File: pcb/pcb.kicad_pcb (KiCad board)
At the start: 2 copper layers, 57 x 84 mm, 4 parts, among them J1 Botones, J2 Pedales+Velocimetro+Monedas, J3 Volante

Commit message: Add layout and schematic prints
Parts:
- moved A1 70.9 mm to (99.1, 147.3)
- moved J1 70.9 mm to (89.9, 179.1)
- moved J2 70.9 mm to (109.2, 102.4)
- moved J3 70.9 mm to (106.7, 111.8)
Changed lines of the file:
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@@
     (thickness 1.6)
   )
-  (paper "A4")
+  (paper "A4" portrait)
+  (title_block
+    (title "Ches Pur Ofi")
+    (date "3/2021")
+    (rev "V1")
+  )
   (layers
     (0 "F.Cu" signal)
@@
   (net 32 "Net-(A1-Pad32)")
   (footprint "Connector_PinSocket_2.54mm:PinSocket_1x03_P2.54mm_Vertical" (layer "F.Cu")
-    (at 157.48 62.23 90)
+    (at 106.68 111.76 90)
     (descr "Through hole straight socket strip, 1x03, 2.54mm pitch, single row (from Kicad 4.0.7), script generated")
     (tags "Through hole socket strip THT 1x03 2.54mm single row")
@@
   )
   (footprint "luqas11:Arduino_Leonardo_WithFemaleSockets" (layer "F.Cu")
-    (at 149.86 97.79)
+    (at 99.06 147.32)
     (attr through_hole)
     (fp_text reference "A1" (at 0 0.5) (layer "F.SilkS")
@@
   )
   (footprint "Connector_PinSocket_2.54mm:PinSocket_1x08_P2.54mm_Vertical" (layer "F.Cu")
-    (at 140.716 129.54 90)
+    (at 89.916 179.07 90)
     (descr "Through hole straight socket strip, 1x08, 2.54mm pitch, single row (from Kicad 4.0.7), script generated")
     (tags "Through hole socket strip THT 1x08 2.54mm single row")
@@
   )
   (footprint "Connector_PinSocket_2.54mm:PinSocket_1x06_P2.54mm_Vertical" (layer "F.Cu")
-    (at 160.02 52.832 90)
+    (at 109.22 102.362 90)
     (descr "Through hole straight socket strip, 1x06, 2.54mm pitch, single row (from Kicad 4.0.7), script generated")
     (tags "Through hole socket strip THT 1x06 2.54mm single row")
@@
     )
   )
-  (gr_line (start 128 49) (end 185 49)
+  (gr_line (start 77.2 98.53) (end 134.2 98.53)
     (stroke (width 0.1) (type solid)) (layer "Edge.Cuts"))
-  (gr_line (start 185 49) (end 185 133)
+  (gr_line (start 134.2 98.53) (end 134.2 182.53)
     (stroke (width 0.1) (type solid)) (layer "Edge.Cuts"))
-  (gr_line (start 185 133) (end 128 133)
+  (gr_line (start 134.2 182.53) (end 77.2 182.53)
     (stroke (width 0.1) (type solid)) (layer "Edge.Cuts"))
-  (gr_line (start 128 133) (end 128 49)
+  (gr_line (start 77.2 182.53) (end 77.2 98.53)
     (stroke (width 0.1) (type solid)) (layer "Edge.Cuts"))
-  (gr_text "V1 - 3/2021" (at 173 129) (layer "B.Cu")
+  (gr_text "V1 - 3/2021" (at 122.2 178.53) (layer "B.Cu")
     (effects (font (size 2 2) (thickness 0.5)) (justify mirror))
   )
-  (gr_text "DAYTONA" (at 154 94) (layer "B.Cu")
+  (gr_text "DAYTONA" (at 103.2 143.53) (layer "B.Cu")
     (effects (font (size 7 7) (thickness 1.3) italic) (justify mirror))
   )
-  (segment (start 138.18 127.004) (end 140.716 129.54) (width 1) (layer "B.Cu") (net 5))
-  (segment (start 138.18 120.65) (end 138.18 127.004) (width 1) (layer "B.Cu") (net 5))
-  (segment (start 143.26 129.536) (end 143.256 129.54) (width 1) (layer "B.Cu") (net 9))
-  (segment (start 143.26 120.65) (end 143.26 129.536) (width 1) (layer "B.Cu") (net 9))
-  (segment (start 167.64 53.34) (end 167.64 72.39) (width 1) (layer "B.Cu") (net 10))
-  (segment (start 145.8 120.65) (end 145.8 129.536) (width 1) (layer "B.Cu") (net 11))
-  (segment (start 145.8 129.536) (end 145.796 129.54) (width 1) (layer "B.Cu") (net 11))
-  (segment (start 165.1 53.34) (end 165.1 72.39) (width 1) (layer "B.Cu") (net 12))
-  (segment (start 148.34 120.65) (end 148.34 129.536) (width 1) (layer "B.Cu") (net 13))
-  (segment (start 148.34 129.536) (end 148.336 129.54) (width 1) (layer "B.Cu") (net 13))
-  (segment (start 162.56 62.23) (end 162.56 72.39) (width 1) (layer "B.Cu") (net 14))
-  (segment (start 150.88 129.536) (end 150.876 129.54) (width 1) (layer "B.Cu") (net 15))
-  (segment (start 150.88 120.65) (end 150.88 129.536) (width 1) (layer "B.Cu") (net 15))
-  (segment (start 153.42 120.65) (end 153.42 129.536) (width 1) (layer "B.Cu") (net 17))
-  (segment (start 153.42 129.536) (end 153.416 129.54) (width 1) (layer "B.Cu") (net 17))
-  (segment (start 160.02 62.23) (end 160.02 67.31) (width 1) (layer "B.Cu") (net 18))
-  (segment (start 162.56 59.69) (end 160.02 62.23) (width 1) (layer "B.Cu") (net 18))
-  (segment (start 162.56 53.34) (end 162.56 59.69) (width 1) (layer "B.Cu") (net 18))
-  (segment (start 160.02 67.31) (end 154.94 72.39) (width 1) (layer "B.Cu") (net 18))
-  (segment (start 155.956 122.174) (end 155.956 129.54) (width 1) (layer "B.Cu") (net 19))
-  (segment (start 157.48 120.65) (end 155.956 122.174) (width 1) (layer "B.Cu") (net 19))
-  (segment (start 160.02 120.65) (end 158.496 122.174) (width 1) (layer "B.Cu") (net 21))
-  (segment (start 158.496 122.174) (end 158.496 129.54) (width 1) (layer "B.Cu") (net 21))
-  (segment (start 160.02 53.34) (end 160.02 59.69) (width 1) (layer "B.Cu") (net 22))
-  (segment (start 157.48 62.23) (end 157.48 64.77) (width 1) (layer "B.Cu") (net 22))
-  (segment (start 150.179998 72.39) (end 149.86 72.39) (width 1) (layer "B.Cu") (net 22))
-  (segment (start 160.02 59.69) (end 157.48 62.23) (width 1) (layer "B.Cu") (net 22))
-  (segment (start 157.48 64.77) (end 149.86 72.39) (width 1) (layer "B.Cu") (net 22))
-  (segment (start 170.18 53.34) (end 180.34 63.5) (width 1) (layer "B.Cu") (net 23))
-  (segment (start 180.34 63.5) (end 180.34 102.87) (width 1) (layer "B.Cu") (net 23))
-  (segment (start 180.34 102.87) (end 162.56 120.65) (width 1) (layer "B.Cu") (net 23))
-  (segment (start 182.372 103.378) (end 165.1 120.65) (width 1) (layer "B.Cu") (net 25))
-  (segment (start 182.372 62.484) (end 182.372 103.378) (width 1) (layer "B.Cu") (net 25))
-  (segment (start 172.72 52.832) (end 182.372 62.484) (width 1) (layer "B.Cu") (net 25))
+  (segment (start 87.38 176.534) (end 89.916 179.07) (width 1) (layer "B.Cu") (net 5))
+  (segment (start 87.38 170.18) (end 87.38 176.534) (width 1) (layer "B.Cu") (net 5))
+  (segment (start 92.46 179.066) (end 92.456 179.07) (width 1) (layer "B.Cu") (net 9))
+  (segment (start 92.46 170.18) (end 92.46 179.066) (width 1) (layer "B.Cu") (net 9))
+  (segment (start 116.84 102.87) (end 116.84 121.92) (width 1) (layer "B.Cu") (net 10))
+  (segment (start 95 170.18) (end 95 179.066) (width 1) (layer "B.Cu") (net 11))
+  (segment (start 95 179.066) (end 94.996 179.07) (width 1) (layer "B.Cu") (net 11))
+  (segment (start 114.3 102.87) (end 114.3 121.92) (width 1) (layer "B.Cu") (net 12))
+  (segment (start 97.54 170.18) (end 97.54 179.066) (width 1) (layer "B.Cu") (net 13))
+  (segment (start 97.54 179.066) (end 97.536 179.07) (width 1) (layer "B.Cu") (net 13))
+  (segment (start 111.76 111.76) (end 111.76 121.92) (width 1) (layer "B.Cu") (net 14))
+  (segment (start 100.08 179.066) (end 100.076 179.07) (width 1) (layer "B.Cu") (net 15))
+  (segment (start 100.08 170.18) (end 100.08 179.066) (width 1) (layer "B.Cu") (net 15))
+  (segment (start 102.62 170.18) (end 102.62 179.066) (width 1) (layer "B.Cu") (net 17))
+  (segment (start 102.62 179.066) (end 102.616 179.07) (width 1) (layer "B.Cu") (net 17))
+  (segment (start 109.22 111.76) (end 109.22 116.84) (width 1) (layer "B.Cu") (net 18))
+  (segment (start 111.76 109.22) (end 109.22 111.76) (width 1) (layer "B.Cu") (net 18))
+  (segment (start 111.76 102.87) (end 111.76 109.22) (width 1) (layer "B.Cu") (net 18))
+  (segment (start 109.22 116.84) (end 104.14 121.92) (width 1) (layer "B.Cu") (net 18))
+  (segment (start 105.156 171.704) (end 105.156 179.07) (width 1) (layer "B.Cu") (net 19))
+  (segment (start 106.68 170.18) (end 105.156 171.704) (width 1) (layer "B.Cu") (net 19))
+  (segment (start 109.22 170.18) (end 107.696 171.704) (width 1) (layer "B.Cu") (net 21))
+  (segment (start 107.696 171.704) (end 107.696 179.07) (width 1) (layer "B.Cu") (net 21))
+  (segment (start 109.22 102.87) (end 109.22 109.22) (width 1) (layer "B.Cu") (net 22))
+  (segment (start 106.68 111.76) (end 106.68 114.3) (width 1) (layer "B.Cu") (net 22))
+  (segment (start 99.379998 121.92) (end 99.06 121.92) (width 1) (layer "B.Cu") (net 22))
+  (segment (start 109.22 109.22) (end 106.68 111.76) (width 1) (layer "B.Cu") (net 22))
+  (segment (start 106.68 114.3) (end 99.06 121.92) (width 1) (layer "B.Cu") (net 22))
+  (segment (start 119.38 102.87) (end 129.54 113.03) (width 1) (layer "B.Cu") (net 23))
+  (segment (start 129.54 113.03) (end 129.54 152.4) (width 1) (layer "B.Cu") (net 23))
+  (segment (start 129.54 152.4) (end 111.76 170.18) (width 1) (layer "B.Cu") (net 23))
+  (segment (start 131.572 152.908) (end 114.3 170.18) (width 1) (layer "B.Cu") (net 25))
+  (segment (start 131.572 112.014) (end 131.572 152.908) (width 1) (layer "B.Cu") (net 25))
+  (segment (start 121.92 102.362) (end 131.572 112.014) (width 1) (layer "B.Cu") (net 25))
   (zone (net 0) (net_name "") (layer "B.Cu") (hatch edge 0.508)
     (connect_pads (clearance 2))
@@
     (polygon
       (pts
-        (xy 185 133)
-        (xy 128 133)
-        (xy 128 49)
-        (xy 185 49)
+        (xy 134.2 182.53)
+        (xy 77.2 182.53)
+        (xy 77.2 98.53)
+        (xy 134.2 98.53)
       )
     )

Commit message: Change footprints folder name
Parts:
- A1: footprint luqas11:Arduino_Leonardo_WithFemaleSockets -> Custom_Footprints:Arduino_Leonardo
- J1: value Botones -> Shifts
- J2: value Pedales+Velocimetro+Monedas -> Pedals+Speedometer+CoinsInput
- J3: value Volante -> Steering
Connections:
- A1 pad 1: Net-(A1-Pad1) -> unconnected-(A1-NC-Pad1)
- A1 pad 12: Net-(A1-Pad12) -> unconnected-(A1-A3-Pad12)
- A1 pad 13: Net-(A1-Pad13) -> unconnected-(A1-A4-Pad13)
- A1 pad 14: Net-(A1-Pad14) -> unconnected-(A1-A5-Pad14)
- A1 pad 15: Net-(A1-Pad15) -> unconnected-(A1-D0/RX-Pad15)
- A1 pad 16: Net-(A1-Pad16) -> unconnected-(A1-D1/TX-Pad16)
- A1 pad 17: Net-(A1-Pad17) -> unconnected-(A1-D2/SDA-Pad17)
- A1 pad 18: Net-(A1-Pad18) -> unconnected-(A1-D3/SCL-Pad18)
- A1 pad 2: Net-(A1-Pad2) -> unconnected-(A1-IOREF-Pad2)
- A1 pad 28: Net-(A1-Pad28) -> unconnected-(A1-D13-Pad28)
- A1 pad 3: Net-(A1-Pad3) -> unconnected-(A1-~{RESET}-Pad3)
- A1 pad 30: Net-(A1-Pad30) -> unconnected-(A1-AREF-Pad30)
- A1 pad 31: Net-(A1-Pad31) -> unconnected-(A1-SDA/D2-Pad31)
- A1 pad 32: Net-(A1-Pad32) -> unconnected-(A1-SCL/D3-Pad32)
- A1 pad 4: Net-(A1-Pad4) -> unconnected-(A1-3V3-Pad4)
- A1 pad 6: Net-(A1-Pad6) -> unconnected-(A1-GND-Pad6)
- A1 pad 8: Net-(A1-Pad8) -> unconnected-(A1-VIN-Pad8)

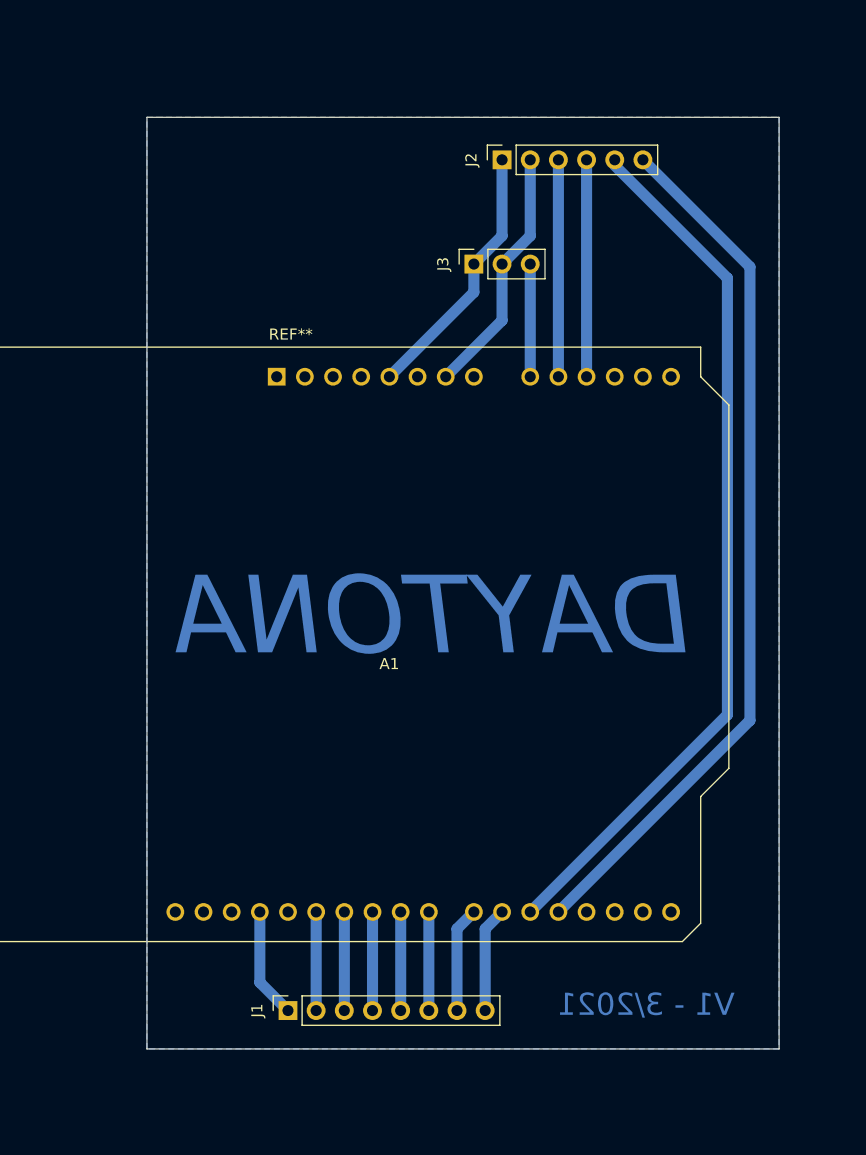
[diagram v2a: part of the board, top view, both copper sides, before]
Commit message: Add new PCB support and update PCB layout
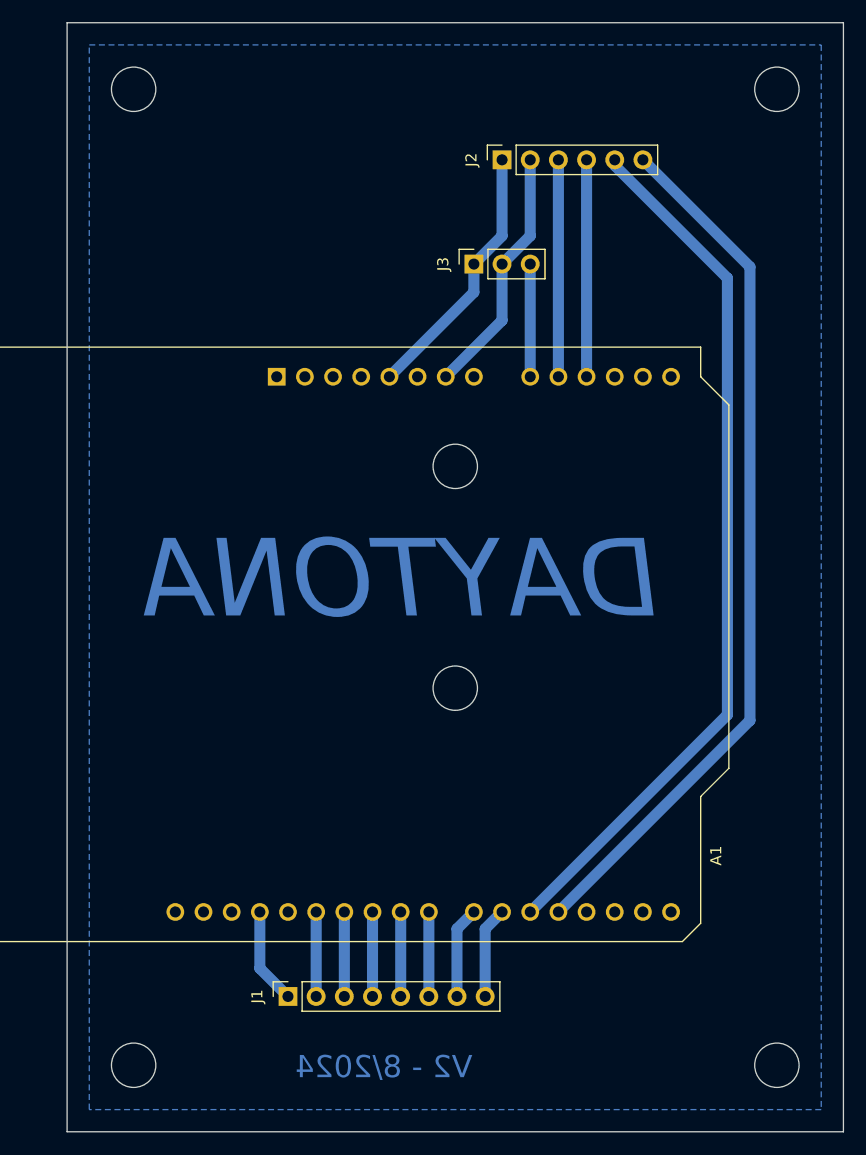
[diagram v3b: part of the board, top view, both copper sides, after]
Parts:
- added REF**: MountingHole_4mm, MountingHole:MountingHole_4mm, F.Cu at (105.0, 150.0)
- added REF**: MountingHole_4mm, MountingHole:MountingHole_4mm, F.Cu at (76.0, 96.0)
- added REF**: MountingHole_4mm, MountingHole:MountingHole_4mm, F.Cu at (134.0, 96.0)
- added REF**: MountingHole_4mm, MountingHole:MountingHole_4mm, F.Cu at (76.0, 184.0)
- added REF**: MountingHole_4mm, MountingHole:MountingHole_4mm, F.Cu at (105.0, 130.0)
- added REF**: MountingHole_4mm, MountingHole:MountingHole_4mm, F.Cu at (134.0, 184.0)
- moved J1 1.27 mm to (89.9, 177.8)
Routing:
- net Net-(A1-D9): track 8.89 -> 7.62 mm
- net Net-(A1-D8): track 8.89 -> 7.62 mm
- net Net-(A1-D11): track 8.89 -> 7.62 mm
- net Net-(A1-D10): track 8.89 -> 7.62 mm
- net Net-(A1-D12): track 8.89 -> 7.62 mm
- net Net-(J1-Pin_1): track 9.94 -> 8.67 mm
- net Net-(A1-D7): track 9.52 -> 8.25 mm
- net Net-(A1-D6): track 9.52 -> 8.25 mm
- net Net-(J2-Pin_2): track 22.2 -> 22.7 mm
- net Net-(A1-D5): track 78.9 -> 79.4 mm
- net Net-(A1-A2): track 19.0 -> 19.6 mm
- net Net-(A1-A1): track 19.0 -> 19.6 mm
- net Net-(A1-+5V): track 23.6 -> 24.1 mm
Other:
- board size 57 x 84 mm -> 70 x 100 mm
- board text added: "V2 - 8/2024"
- board text removed: "V1 - 3/2021"
